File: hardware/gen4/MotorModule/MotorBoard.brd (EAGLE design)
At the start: 34 x 61.7 mm, 65 parts, among them IC1 XMEGA16A4A, IC2 3.3V REG, M1O1 TEST_PT, M1O2 TEST_PT, M1O3 TEST_PT

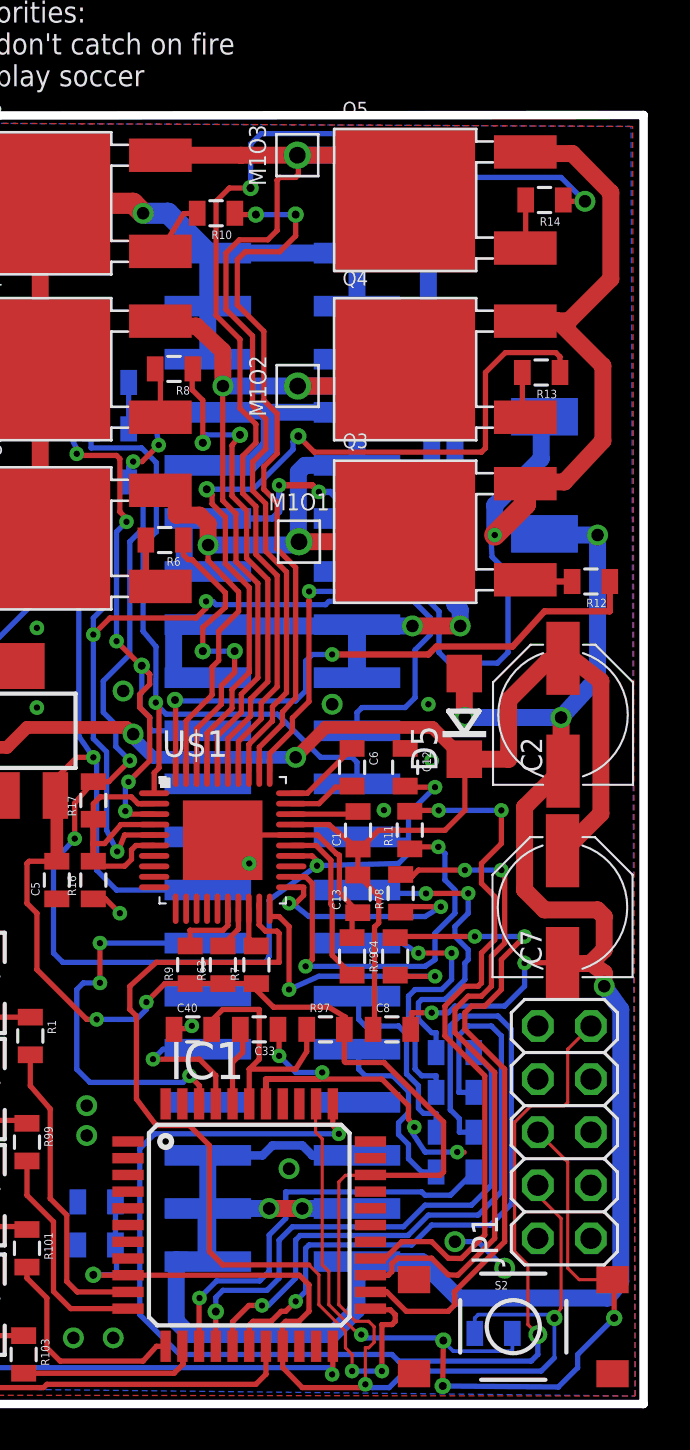
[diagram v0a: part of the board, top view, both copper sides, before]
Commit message: motorboard ground connections fixes
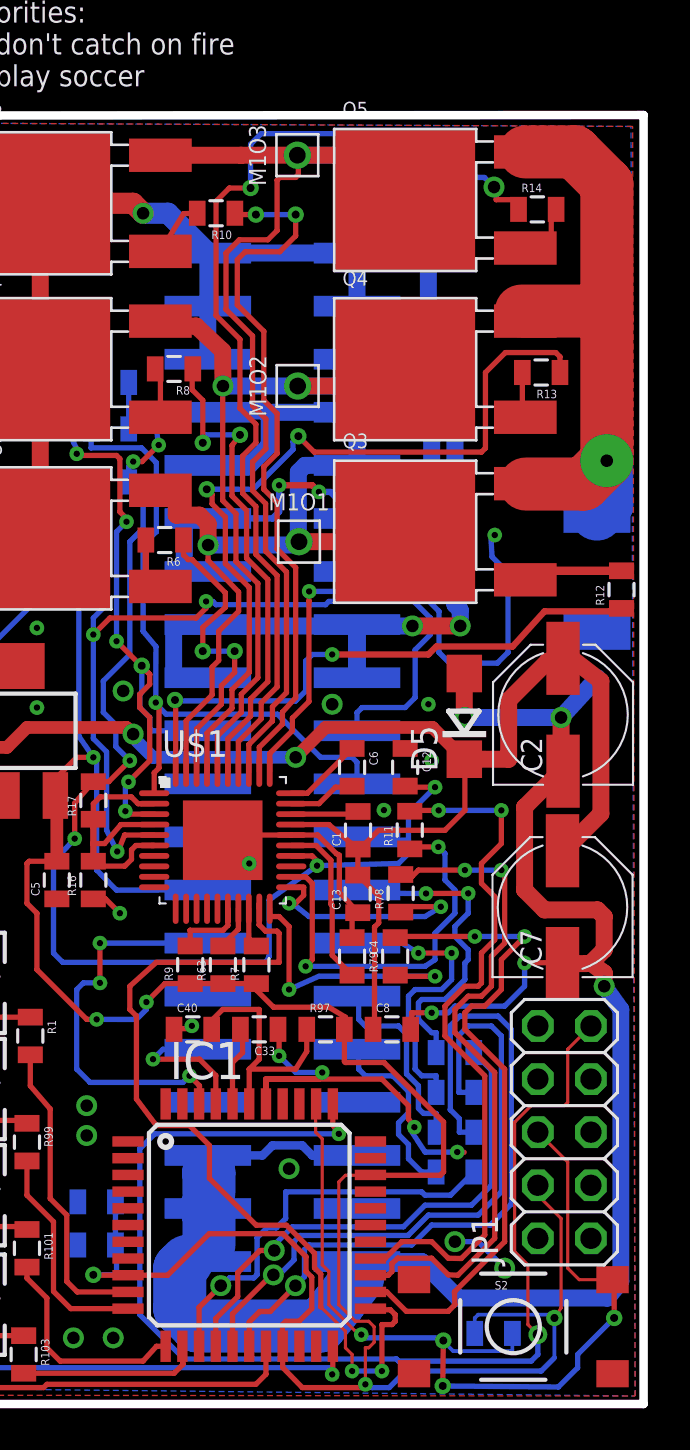
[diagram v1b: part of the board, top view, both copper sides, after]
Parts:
- moved R18 5.29 mm to (30.9, 23.1)
- moved R12 1.52 mm to (32.1, 22.3), turned to 90 degrees
- moved R14 0.57 mm to (28.1, 40.5), turned to 0 degrees
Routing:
- net 12VGND: track 115.6 -> 97.9 mm, vias 8 -> 5
- net O1: track 63.3 -> 58.0 mm, vias 2 -> 3
- net N$17: track 52.4 -> 49.0 mm
- net 3.3V: track 123.7 -> 126.1 mm
- net N$11: track 3.04 -> 5.44 mm
- net PWM1: track 43.5 -> 41.9 mm
- net N$14: track 2.31 -> 3.31 mm
- net N$19: track 28.4 -> 27.5 mm
- net MOSI: track 25.5 -> 24.7 mm

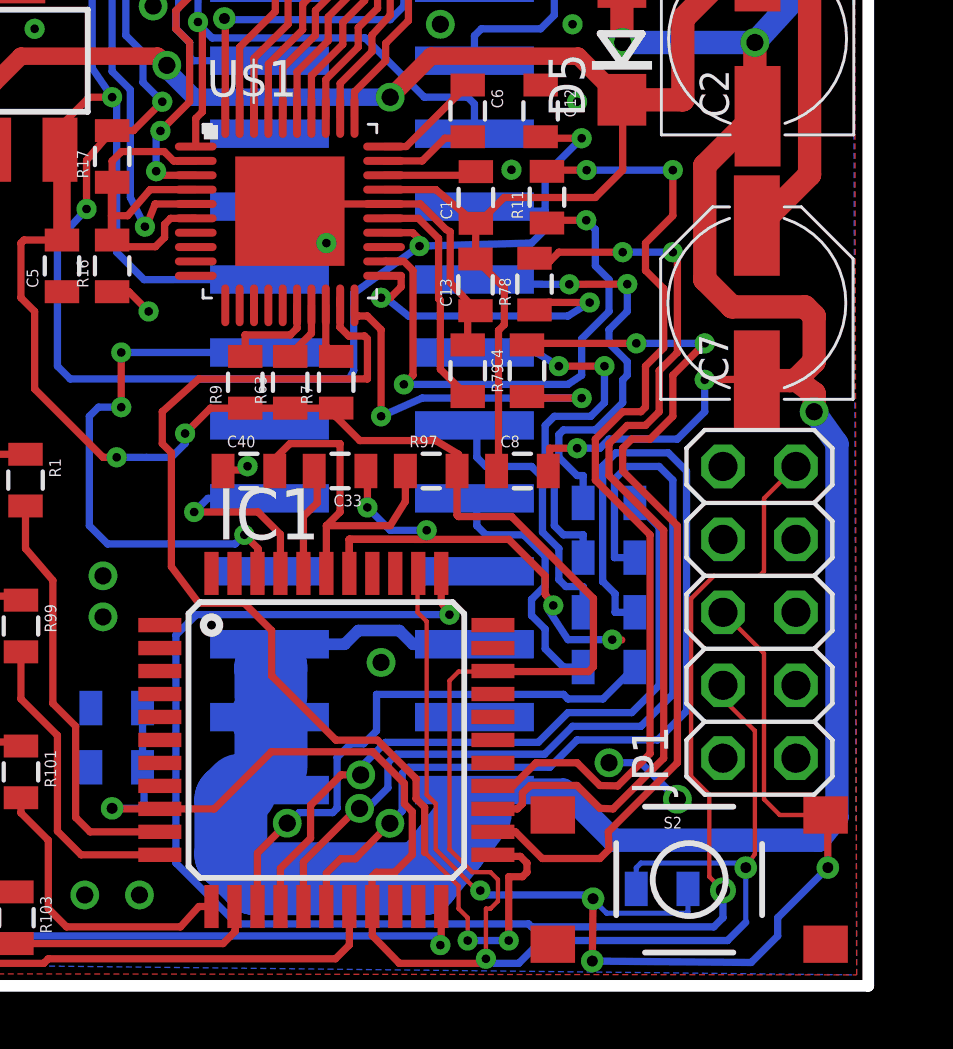
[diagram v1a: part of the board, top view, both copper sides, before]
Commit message: an experiment with ground connections on motorboard - reverse if necessary
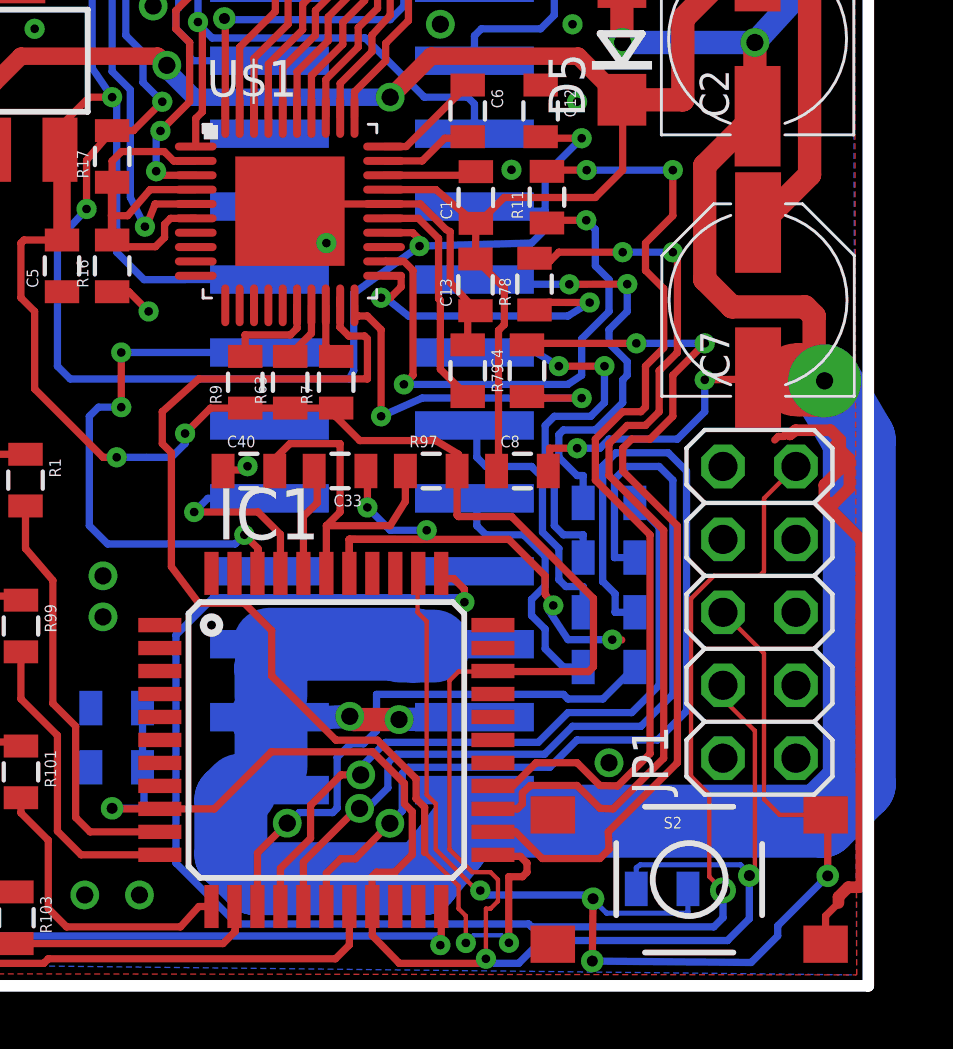
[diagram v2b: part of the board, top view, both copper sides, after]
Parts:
- moved C7 0.11 mm to (29.3, 7.22)
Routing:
- net GND: track 58.4 -> 79.9 mm, vias 21 -> 19
- net 12VGND: track 97.9 -> 105.7 mm, vias 5 -> 7
- net DATA: track 58.0 -> 58.8 mm

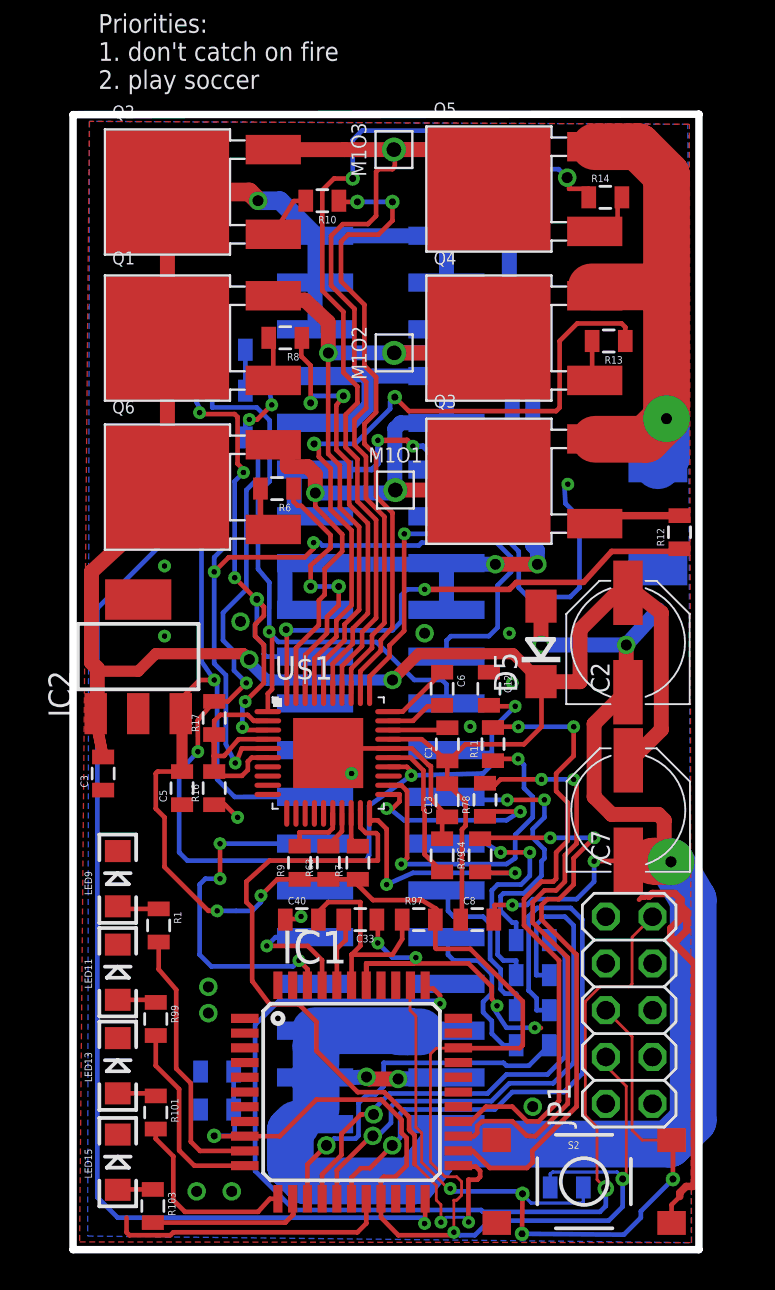
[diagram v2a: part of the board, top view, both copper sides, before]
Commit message: finished increasing trace width on motorboard
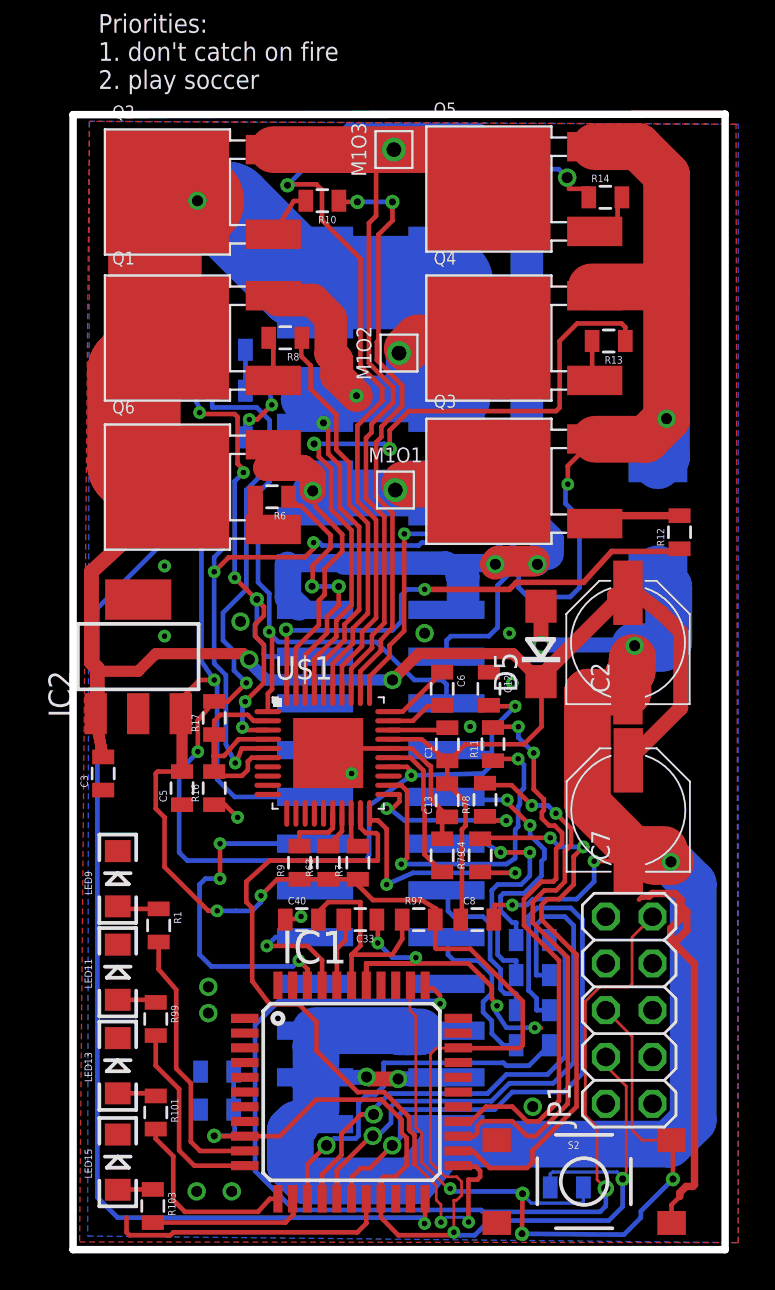
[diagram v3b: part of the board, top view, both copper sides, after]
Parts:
- moved R6 0.52 mm to (9.97, 24.2)
- moved M1O2 0.26 mm to (16.9, 32.0)
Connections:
- net M1O1: now also JP3.11, JP3.12, JP3.13, JP3.14; no longer JP3.10, JP3.7, JP3.8, JP3.9
- net M1O2: now also JP3.10, JP3.7, JP3.8, JP3.9; no longer JP3.11, JP3.12, JP3.13, JP3.14
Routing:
- net M1O2: track 68.1 -> 50.9 mm, vias 3 -> 2
- net 12VGND: track 105.7 -> 111.8 mm
- net M1O1: track 47.9 -> 42.4 mm
- net N$17: track 49.0 -> 52.4 mm
- net 12V: track 130.8 -> 134.0 mm
- net O1: track 58.0 -> 60.9 mm
- net ENABLE: track 34.4 -> 31.9 mm
- net DIR: track 32.4 -> 30.2 mm
- net N$20: track 23.6 -> 21.6 mm, vias 2 -> 0
- net N$21: track 34.1 -> 32.2 mm
- net N$45: track 15.6 -> 13.9 mm
- net BREN: track 31.7 -> 30.6 mm
- net N$98: track 11.4 -> 10.5 mm
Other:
- board size 34 x 61.7 mm -> 35.4 x 61.7 mm

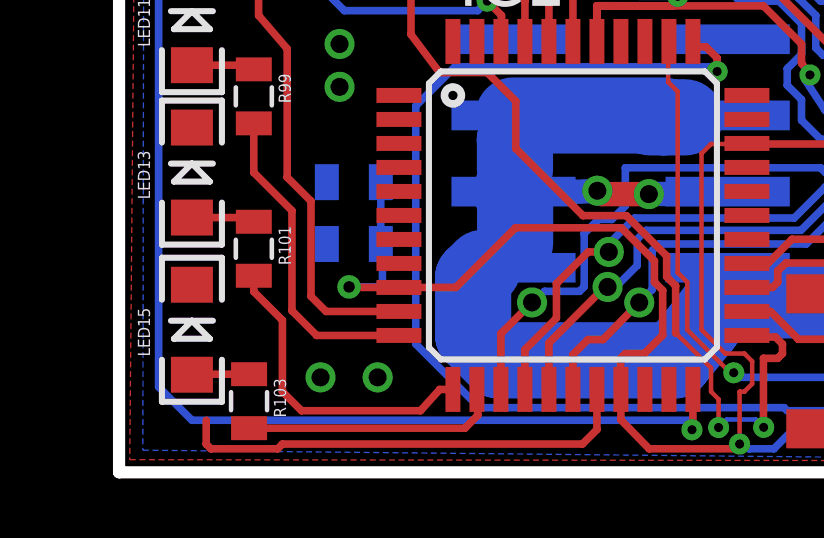
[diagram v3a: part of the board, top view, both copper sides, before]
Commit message: added ferrite beads
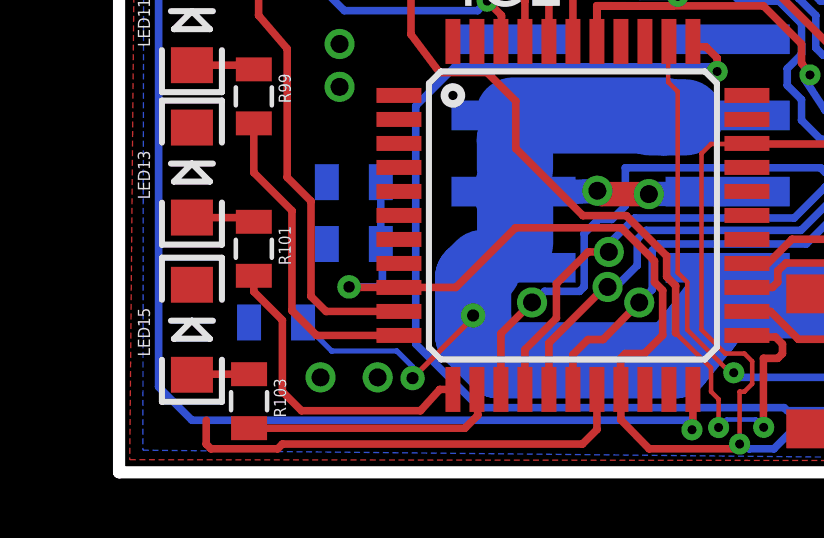
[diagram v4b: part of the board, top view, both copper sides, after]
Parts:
- added U$2: INDUCTOR, gen3:0805
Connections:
- net 12VGND: now also U$2.1
- net GND: now also U$2.2
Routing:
- net 12VGND: track 111.8 -> 119.4 mm, vias 7 -> 9
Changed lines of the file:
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@@
 <element name="R18" library="resistor" package="R2512" value="0.05" x="30.927684375" y="23.127403125" rot="MR90"/>
 <element name="JP1" library="pinhead" package="2X05" value="DEBUG" x="29.36875" y="-3.65125" rot="R90"/>
+<element name="U$2" library="gen3" package="0805" value="INDUCTOR" x="4.392165625" y="-11.6639" rot="MR0"/>
 </elements>
 <signals>
@@
 <wire x1="30.202521875" y1="2.4735875" x2="30.023528125" y2="2.4735875" width="0.254" layer="1"/>
 <wire x1="30.023528125" y1="2.4735875" x2="29.901475" y2="2.351534375" width="0.254" layer="1"/>
+<contactref element="U$2" pad="2"/>
 </signal>
 <signal name="MOSI">
@@
 <wire x1="17.673990625" y1="-12.927690625" x2="11.806784375" y2="-12.927690625" width="2.54" layer="16"/>
 <wire x1="11.806784375" y1="-12.927690625" x2="10.960425" y2="-12.08133125" width="2.54" layer="16"/>
-<wire x1="10.960425" y1="-12.08133125" x2="10.960425" y2="-10.17375" width="2.54" layer="16"/>
+<wire x1="10.960425" y1="-12.08133125" x2="10.960425" y2="-11.511759375" width="2.54" layer="16"/>
+<wire x1="10.960425" y1="-11.511759375" x2="10.960425" y2="-11.430371875" width="2.54" layer="16"/>
+<wire x1="10.960425" y1="-11.430371875" x2="10.960425" y2="-10.17375" width="2.54" layer="16"/>
 <wire x1="10.960425" y1="-10.17375" x2="11.291675" y2="-9.8425" width="2.54" layer="16"/>
 <wire x1="19.4437" y1="-4.7625" x2="18.0937375" y2="-4.7625" width="0.254" layer="16"/>
@@
 <via x="31.636946875" y="4.41064375" extent="1-16" drill="0.6"/>
 <wire x1="31.636946875" y1="4.41064375" x2="32.845646875" y2="3.20194375" width="2.54" layer="16"/>
+<contactref element="U$2" pad="1"/>
+<wire x1="5.292165625" y1="-11.6639" x2="6.243271875" y2="-12.61500625" width="0.1778" layer="16"/>
+<wire x1="6.243271875" y1="-12.61500625" x2="8.418296875" y2="-12.61500625" width="0.1778" layer="16"/>
+<wire x1="8.418296875" y1="-12.61500625" x2="8.94274375" y2="-13.139453125" width="0.1778" layer="16"/>
+<wire x1="8.94274375" y1="-13.139453125" x2="8.94274375" y2="-13.51930625" width="0.1778" layer="16"/>
+<via x="8.94274375" y="-13.51930625" extent="1-16" drill="0.4064"/>
+<wire x1="8.94274375" y1="-13.51930625" x2="10.960425" y2="-11.501625" width="0.1778" layer="1"/>
+<wire x1="10.960425" y1="-11.501625" x2="10.960425" y2="-11.430371875" width="0.1778" layer="1"/>
+<via x="10.960425" y="-11.430371875" extent="1-16" drill="0.4064"/>
 </signal>
 <signal name="M1QB">
